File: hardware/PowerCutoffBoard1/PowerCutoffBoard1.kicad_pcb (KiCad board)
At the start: 2 copper layers, 50 x 60 mm, 51 parts, among them J1 Conn_Coaxial, J2 Conn_01x03, J3 Conn_01x04, J4 Conn_01x04, J5 Conn_01x04, J6 Conn_01x04, SW1 SW_Push, SW2 SW_Push, SW3 SW_DIP_x04, U1 STM32F303K8Tx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

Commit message: update
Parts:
- removed C12, C14: 10u, Capacitor_SMD:C_0805_2012Metric_Pad1.18x1.45mm_HandSolder
- removed J4: Conn_01x04, Connector_JST:JST_XH_S4B-XH-A_1x04_P2.50mm_Horizontal
- removed the REF** at (103.5, 93.5)
- removed the REF** at (146.5, 93.5)
- removed the REF** at (146.5, 146.5)
- removed the REF** at (103.5, 146.5)
- added R3: 120, Resistor_SMD:R_0603_1608Metric_Pad0.98x0.95mm_HandSolder, F.Cu at (184.9, 138.6)
- added REF**: MountingHole_3.2mm_M3, MountingHole:MountingHole_3.2mm_M3, F.Cu at (153.0, 108.0)
- added REF**: MountingHole_3.2mm_M3, MountingHole:MountingHole_3.2mm_M3, F.Cu at (153.0, 147.0)
- added REF**: MountingHole_3.2mm_M3, MountingHole:MountingHole_3.2mm_M3, F.Cu at (197.0, 108.0)
- added REF**: MountingHole_3.2mm_M3, MountingHole:MountingHole_3.2mm_M3, F.Cu at (197.0, 147.0)
- added Y1: Crystal_GND2, Crystal:Resonator_SMD_Murata_CSTxExxV-3Pin_3.0x1.1mm_HandSoldering, F.Cu at (181.1, 121.8)
- moved J2 86.2 mm to (192.0, 123.4), turned to -90 degrees
- moved J3 83.1 mm to (190.4, 139.8), turned to 90 degrees
- moved C10 78.0 mm to (188.2, 114.8), turned to 0 degrees
- moved C9 78.0 mm to (188.2, 116.3), turned to 0 degrees
- moved C11 72.4 mm to (185.8, 141.0), turned to 0 degrees
- moved U4 67.1 mm to (182.8, 115.7), turned to 0 degrees
- moved U5 60.7 mm to (180.3, 138.6), turned to 0 degrees
- moved R1 60.2 mm to (186.4, 127.9)
- moved C3 57.4 mm to (174.9, 135.8)
- moved U1 55.2 mm to (179.5, 129.8), turned to -90 degrees
- moved C8 54.7 mm to (160.5, 138.3), turned to 180 degrees
- moved C1 53.9 mm to (184.5, 125.2)
- moved C7 53.6 mm to (168.4, 138.3)
- moved J6 52.8 mm to (177.3, 145.8)
- moved U3 52.7 mm to (163.3, 132.7)
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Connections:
- J6 pad 1: USART2_RX -> USART1_RX
- J6 pad 3: USART2_TX -> USART1_TX
- U1 pad 2: unconnected-(U1-PF0-Pad2) -> Net-(U1-PF0)
- U1 pad 21: CAN_RX -> CANRX
- U1 pad 22: CAN_TX -> CANTX
- U1 pad 3: unconnected-(U1-PF1-Pad3) -> Net-(U1-PF1)
- U2 pad 10: USART1_RX -> USART2_RX
- U2 pad 9: USART1_TX -> USART2_TX
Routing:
- net Net-(J1-In): track 0.00 -> 6.98 mm
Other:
- board size 50 x 60 mm -> 50 x 45 mm

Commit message: update
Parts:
- moved J5 27.2 mm to (177.7, 145.9), turned to 0 degrees
- moved J6 26.9 mm to (153.9, 132.5), turned to -90 degrees
- moved D2 19.3 mm to (178.7, 107.1)
- moved R2 19.3 mm to (178.7, 110.5)
- moved D5 3.68 mm to (182.5, 107.1)
- moved D6 3.68 mm to (185.3, 107.1)
- moved D7 3.68 mm to (188.2, 107.1)
- moved R5 3.68 mm to (182.5, 110.5)
- moved R6 3.68 mm to (185.3, 110.5)
- moved R7 3.68 mm to (188.2, 110.5)
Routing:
- net MCU_SWDIO: track 0.00 -> 20.6 mm
- net RF_LED: track 0.00 -> 17.5 mm
- net OUT_A: track 0.00 -> 12.9 mm
- net MCU_SWCLK: track 0.00 -> 12.8 mm
- net CANH: track 0.00 -> 9.89 mm
- net CANL: track 0.00 -> 8.57 mm
- net CANTX: track 0.00 -> 8.22 mm
- net OUT_B: track 0.00 -> 7.24 mm
- net CANRX: track 0.00 -> 4.43 mm
- net Net-(U1-PF0): track 0.00 -> 4.18 mm
- net Net-(U1-PF1): track 0.00 -> 4.14 mm
- net Net-(U1-BOOT0): track 0.00 -> 1.99 mm
- net MCU_RST: track 0.00 -> 1.43 mm
- added copper zone on B.Cu, net GND
- added copper zone on F.Cu, net GND

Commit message: update
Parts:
- moved D1 38.4 mm to (188.8, 108.6), turned to -90 degrees
- moved D5 37.8 mm to (159.7, 137.2), turned to 0 degrees
- moved C7 37.7 mm to (190.8, 108.0), turned to -90 degrees
- moved D7 37.5 mm to (159.7, 131.4), turned to 0 degrees
- moved D6 37.4 mm to (159.6, 134.4), turned to 0 degrees
- moved C8 34.2 mm to (176.9, 108.3)
- moved R5 33.0 mm to (163.1, 137.2), turned to 180 degrees
- moved R7 32.8 mm to (163.0, 131.4), turned to 180 degrees
- moved R6 32.6 mm to (163.0, 134.4), turned to 180 degrees
- moved U3 30.3 mm to (183.1, 109.9), turned to 180 degrees
- moved D4 27.5 mm to (180.2, 125.2)
- moved R4 27.5 mm to (183.5, 125.2)
- moved J6 20.3 mm to (169.0, 146.2), turned to 0 degrees
- moved R3 19.1 mm to (186.7, 119.5)
- moved U4 18.8 mm to (186.3, 134.1), turned to 90 degrees
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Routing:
- net MCU_SWDIO: track 20.6 -> 0.00 mm
- net RF_LED: track 17.5 -> 0.00 mm
- net OUT_A: track 12.9 -> 0.00 mm
- net MCU_SWCLK: track 12.8 -> 0.00 mm
- net CANH: track 9.89 -> 0.00 mm
- net CANL: track 8.57 -> 0.00 mm
- net CANTX: track 8.22 -> 0.00 mm, vias 0 -> 2
- net OUT_B: track 7.24 -> 0.00 mm
- net Net-(J1-In): track 6.98 -> 0.00 mm
- net CANRX: track 4.43 -> 0.00 mm, vias 0 -> 2
- net Net-(U1-PF0): track 4.18 -> 0.00 mm
- net Net-(U1-PF1): track 4.14 -> 0.00 mm
- net Net-(U1-BOOT0): track 1.99 -> 0.00 mm
- net MCU_RST: track 1.43 -> 0.00 mm
- removed copper zone on B.Cu, net GND
- removed copper zone on F.Cu, net GND

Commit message: PCB:Temporarily correct placement of parts
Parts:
- moved C3 2.09 mm to (169.3, 140.4), turned to -90 degrees
- moved C1 1.04 mm to (176.9, 127.7), turned to 90 degrees
- moved C8 0.83 mm to (177.4, 109.0), turned to 90 degrees
- moved C2 0.68 mm to (169.8, 126.8)
- moved R1 0.53 mm to (179.6, 131.3)
- moved D4 0.29 mm to (180.0, 125.4)
- moved R8 0.20 mm to (178.6, 137.6)
- moved R9 0.19 mm to (180.7, 137.6)
- moved R4 0.18 mm to (183.5, 125.4)
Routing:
- net CANTX: vias 2 -> 1
- net CANRX: vias 2 -> 1

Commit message: update:PCB updated
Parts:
- moved D8 40.5 mm to (142.6, 159.7)
- moved D9 40.5 mm to (144.8, 159.7)
- moved R8 40.5 mm to (142.6, 156.2)
- moved R9 40.5 mm to (144.8, 156.2)
- moved C2 26.5 mm to (145.8, 137.9)
- moved Y1 11.6 mm to (180.0, 134.8), turned to 90 degrees
- moved C3 10.8 mm to (179.8, 137.8), turned to 0 degrees
- moved R1 10.5 mm to (174.1, 140.3), turned to -90 degrees
- moved C1 5.10 mm to (179.8, 131.9), turned to 0 degrees
- moved C5 2.95 mm to (156.3, 128.0), turned to 180 degrees
- moved TP1 1.03 mm to (153.0, 136.0)
- moved R3 0.45 mm to (186.6, 120.0)
- turned U1 to 180 degrees
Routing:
- net MCU_SWDIO: track 0.00 -> 33.1 mm
- net CANTX: track 0.00 -> 27.2 mm, vias 1 -> 2
- net MCU_SWCLK: track 0.00 -> 27.1 mm, vias 0 -> 1
- net CANRX: track 0.00 -> 26.8 mm, vias 1 -> 2
- net MCU_RST: track 0.00 -> 23.2 mm, vias 0 -> 2
- net USART1_TX: track 0.00 -> 22.9 mm
- net USART1_RX: track 0.00 -> 16.7 mm, vias 0 -> 1
- net USART2_RX: track 0.00 -> 15.0 mm, vias 0 -> 2
- net +3.3V: track 0.00 -> 14.5 mm
- net USART2_TX: track 0.00 -> 13.7 mm
- net CANH: track 0.00 -> 9.69 mm
- net OUT_A: track 0.00 -> 7.60 mm
- net CANL: track 0.00 -> 6.77 mm
- net Net-(J1-In): track 0.00 -> 6.20 mm
- net +5V: track 0.00 -> 4.13 mm
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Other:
- board text added: "120ohm"
- board text added: "MCU_RST"

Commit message: fix:schematic
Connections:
- U1 pad 11: unconnected-(U1-PA5-Pad11) -> LED_2
- U1 pad 12: unconnected-(U1-PA6-Pad12) -> LED_1
- U1 pad 13: unconnected-(U1-PA7-Pad13) -> LED_Connection
- U1 pad 14: unconnected-(U1-PB0-Pad14) -> LED_Debug
- U1 pad 15: unconnected-(U1-PB1-Pad15) -> LED_Error
- U1 pad 25: unconnected-(U1-PA15-Pad25) -> DIP_4
- U1 pad 26: unconnected-(U1-PB3-Pad26) -> DIP_3
- U1 pad 27: unconnected-(U1-PB4-Pad27) -> DIP_2
- U1 pad 28: unconnected-(U1-PB5-Pad28) -> DIP_1
- U1 pad 29: unconnected-(U1-PB6-Pad29) -> IN_A
- U1 pad 30: unconnected-(U1-PB7-Pad30) -> IN_B

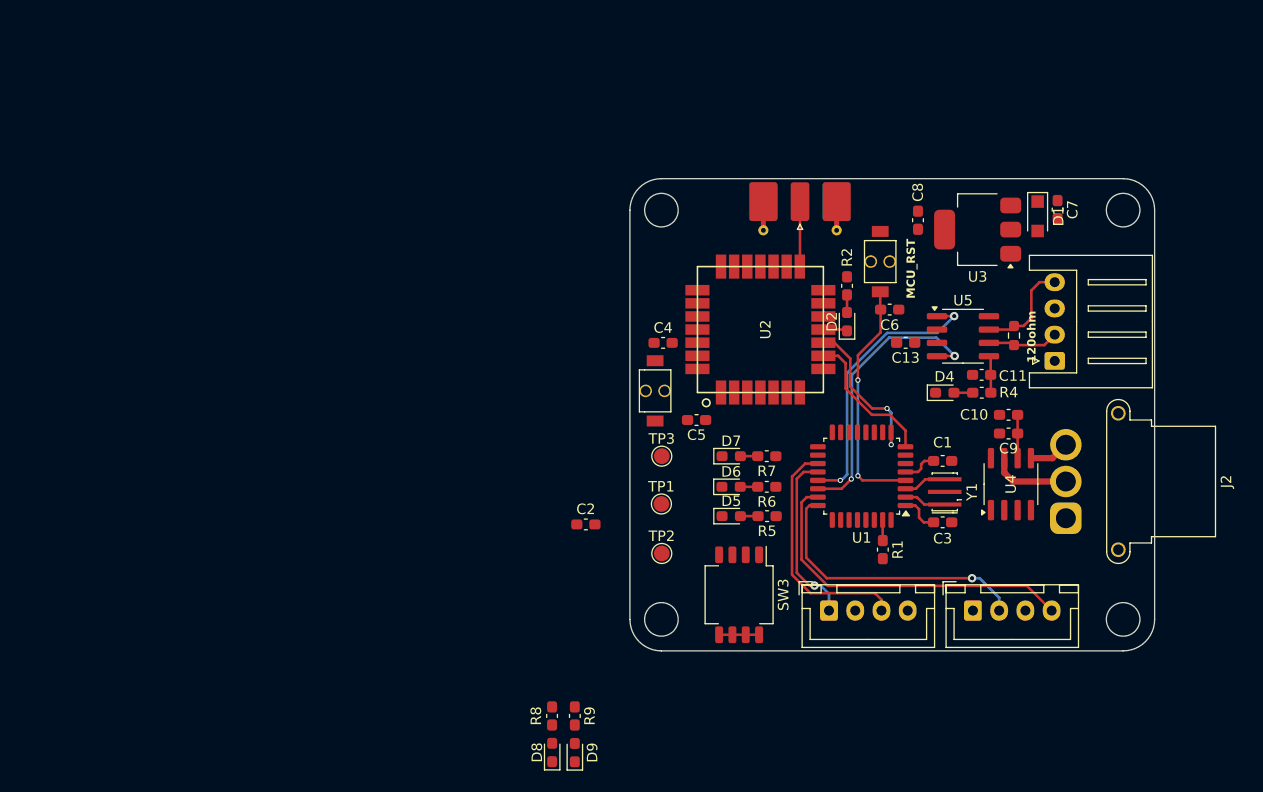
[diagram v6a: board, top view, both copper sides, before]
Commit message: Wired PowerCutoffBoard1
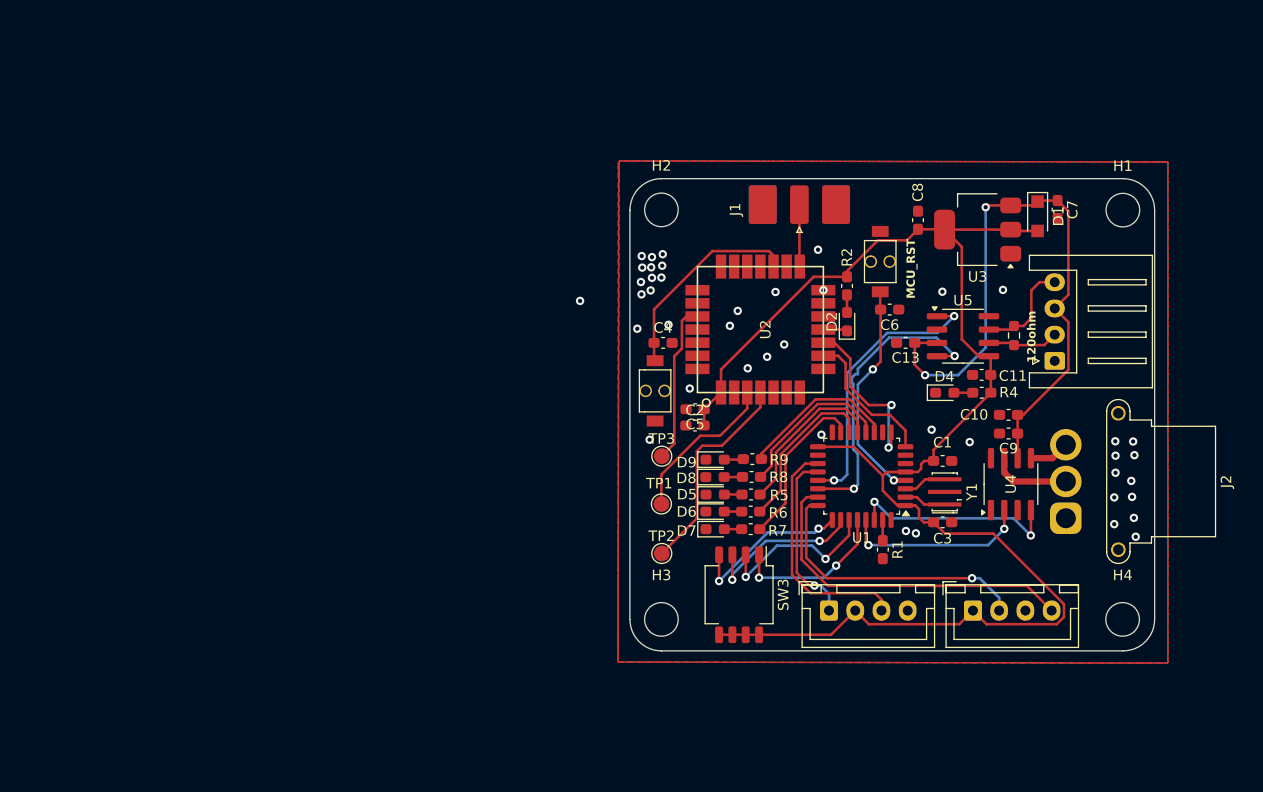
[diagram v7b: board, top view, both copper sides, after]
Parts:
- removed REF** (x4): MountingHole_3.2mm_M3, MountingHole:MountingHole_3.2mm_M3
- added H1: MountingHole, MountingHole:MountingHole_3.2mm_M3, F.Cu at (197.0, 108.0)
- added H2: MountingHole, MountingHole:MountingHole_3.2mm_M3, F.Cu at (153.0, 108.0)
- added H3: MountingHole, MountingHole:MountingHole_3.2mm_M3, F.Cu at (153.0, 147.0)
- added H4: MountingHole, MountingHole:MountingHole_3.2mm_M3, F.Cu at (196.9, 147.0)
- moved D9 31.0 mm to (158.1, 131.8), turned to 0 degrees
- moved D8 30.5 mm to (158.1, 133.4), turned to 0 degrees
- moved R9 29.7 mm to (161.7, 131.7), turned to 180 degrees
- moved R8 29.7 mm to (161.6, 133.4), turned to 180 degrees
- moved C2 14.0 mm to (156.2, 128.5)
- moved R7 7.12 mm to (161.5, 138.4)
- moved D7 7.12 mm to (158.1, 138.4)
- moved R6 2.81 mm to (161.5, 136.7)
- moved D6 2.81 mm to (158.1, 136.7)
- moved R5 2.57 mm to (161.5, 135.1)
- moved D5 2.57 mm to (158.1, 135.1)
- moved C5 1.03 mm to (156.2, 127.0)
- moved J1 0.29 mm to (166.2, 107.2)
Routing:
- net +3.3V: track 14.5 -> 142.4 mm
- net +5V: track 4.13 -> 61.3 mm, vias 0 -> 2
- net IN_B: track 0.00 -> 20.4 mm, vias 0 -> 2
- net RF_SWCLK: track 0.00 -> 20.3 mm
- net RF_RST: track 0.00 -> 19.8 mm
- net IN_A: track 0.00 -> 17.9 mm, vias 0 -> 2
- net DIP_2: track 0.00 -> 16.2 mm, vias 0 -> 2
- net LED_Debug: track 0.00 -> 15.9 mm
- net LED_Connection: track 0.00 -> 15.7 mm
- net DIP_4: track 0.00 -> 15.7 mm, vias 0 -> 2
- net DIP_3: track 0.00 -> 15.7 mm, vias 0 -> 2
- net LED_Error: track 0.00 -> 15.7 mm
- net LED_1: track 0.00 -> 15.5 mm
- net RF_BOOT: track 0.00 -> 15.3 mm
- net DIP_1: track 0.00 -> 15.2 mm, vias 0 -> 2
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- added copper zone on B.Cu, net GND
- added copper zone on F.Cu, net GND

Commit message: RemoteSwitchBoard sch
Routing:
- net CANTX: track 28.5 -> 27.3 mm
